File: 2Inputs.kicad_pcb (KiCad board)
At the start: 2 copper layers, 30.2 x 30.2 mm, 20 parts, among them J1 JST_SH_SM06B-SRSS-TB_1x06-1MP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, J2 Input0, J3 Input1, J4 Conn_01x04, U1 M24C02-FMN

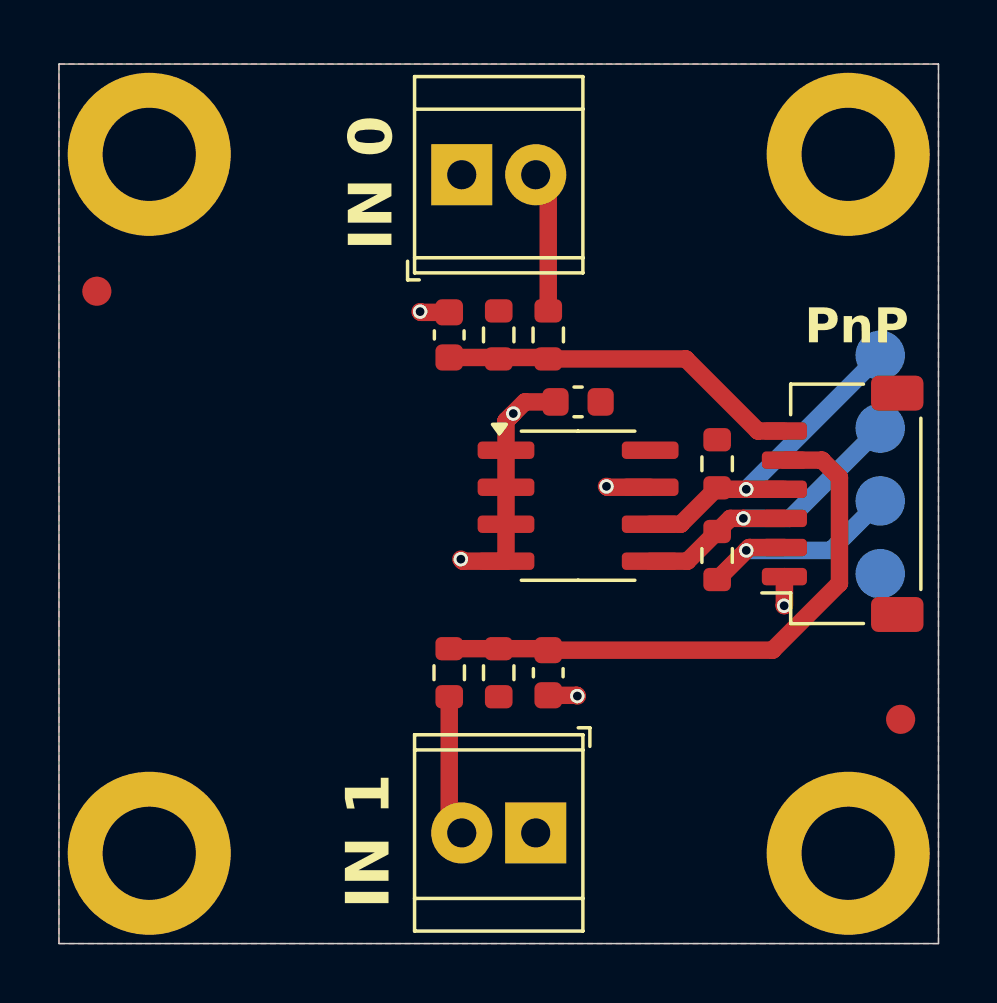
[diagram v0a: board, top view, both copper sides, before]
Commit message: Change screw terminals to 3.5mm version
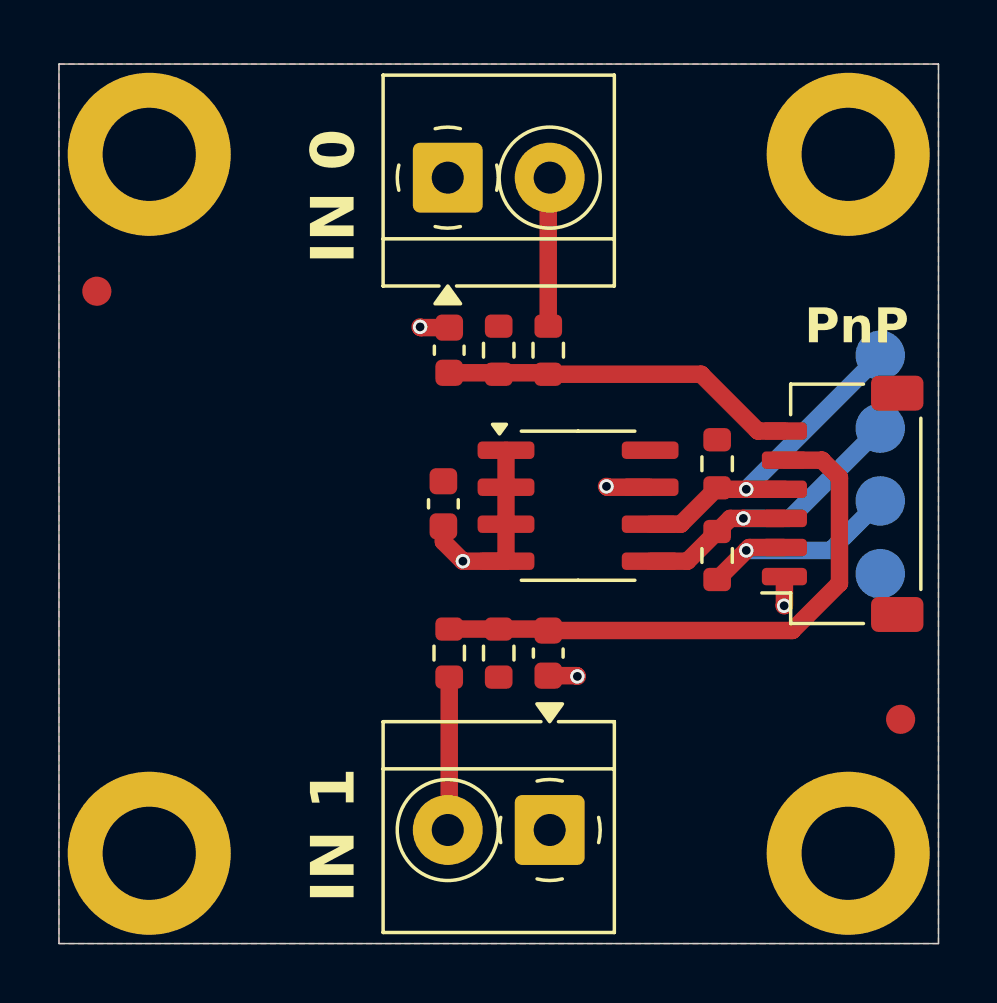
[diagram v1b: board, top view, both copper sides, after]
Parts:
- J2, J3: footprint TerminalBlock_TE-Connectivity:TerminalBlock_TE_282834-2_1x02_P2.54mm_Horizontal -> TerminalBlock_4Ucon:TerminalBlock_4Ucon_1x02_P3.50mm_Horizontal
- moved C1 5.80 mm to (49.7, 47.1), turned to -90 degrees
- moved C3 0.67 mm to (53.3, 52.2)
- moved R3 0.67 mm to (49.9, 52.2)
- moved R4 0.67 mm to (51.6, 52.2)
- moved C2 0.53 mm to (49.9, 41.8)
- moved R1 0.53 mm to (51.6, 41.8)
- moved R2 0.53 mm to (53.3, 41.8)
- moved J2 0.49 mm to (53.4, 58.3)
- moved J3 0.49 mm to (49.9, 35.9)
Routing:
- net GND: track 13.3 -> 11.3 mm, vias 6 -> 5
- net Net-(J2-Pin_2): track 4.85 -> 5.88 mm
- net Net-(J3-Pin_2): track 4.85 -> 5.80 mm
